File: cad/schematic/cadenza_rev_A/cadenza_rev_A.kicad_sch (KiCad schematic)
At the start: 0 parts

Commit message: added the PCB outline first proposal for the part selection
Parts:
- added J1: USB_B, Connector_USB:USB_B_Amphenol_MUSB-D511_Vertical_Rugged, symbol Connector:USB_B
- added U1, U11, U3, U5, U7, U9: TLC5916, Package_SO:TSSOP-16_4.4x5mm_P0.65mm, symbol Driver_LED:TLC5916
- added U10, U12, U2, U4, U6, U8: HDSP-A151, Display_7Segment:HDSP-A151, symbol Display_Character:HDSP-A151
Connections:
- new net: U4.1 (CA), U4.6 (CA)
- new net: U3.5 (~{OUT0}), U4.10 (A)
- new net: U3.10 (~{OUT5}), U4.2 (F)
- new net: U3.11 (~{OUT6}), U4.3 (G)
- new net: U3.9 (~{OUT4}), U4.4 (E)
- new net: U3.8 (~{OUT3}), U4.5 (D)
- new net: U3.12 (~{OUT7}), U4.7 (DP)
- new net: U3.7 (~{OUT2}), U4.8 (C)
- new net: U3.6 (~{OUT1}), U4.9 (B)
- new net: U10.2 (F), U9.10 (~{OUT5})
- new net: U10.3 (G), U9.11 (~{OUT6})
- new net: U10.7 (DP), U9.12 (~{OUT7})
- new net: U1.16 (VDD), U11.16 (VDD), U3.16 (VDD), U5.16 (VDD), U7.16 (VDD), U9.16 (VDD)
- new net: U10.10 (A), U9.5 (~{OUT0})
- new net: U10.9 (B), U9.6 (~{OUT1})
- new net: U10.8 (C), U9.7 (~{OUT2})
- new net: U10.5 (D), U9.8 (~{OUT3})
- new net: U10.4 (E), U9.9 (~{OUT4})
- new net: U7.10 (~{OUT5}), U8.2 (F)
- new net: U7.11 (~{OUT6}), U8.3 (G)
- new net: U7.12 (~{OUT7}), U8.7 (DP)
- new net: U7.5 (~{OUT0}), U8.10 (A)
- new net: U7.6 (~{OUT1}), U8.9 (B)
- new net: U7.7 (~{OUT2}), U8.8 (C)
- new net: U7.8 (~{OUT3}), U8.5 (D)
- new net: U7.9 (~{OUT4}), U8.4 (E)
- new net: U8.1 (CA), U8.6 (CA)
- new net: U6.1 (CA), U6.6 (CA)
- new net: U5.5 (~{OUT0}), U6.10 (A)
- new net: U5.10 (~{OUT5}), U6.2 (F)
- new net: U5.11 (~{OUT6}), U6.3 (G)
- new net: U5.9 (~{OUT4}), U6.4 (E)
- new net: U5.8 (~{OUT3}), U6.5 (D)
- new net: U5.12 (~{OUT7}), U6.7 (DP)
- new net: U5.7 (~{OUT2}), U6.8 (C)
- new net: U5.6 (~{OUT1}), U6.9 (B)
- new net: U1.10 (~{OUT5}), U2.2 (F)
- new net: U1.11 (~{OUT6}), U2.3 (G)
- new net: U1.12 (~{OUT7}), U2.7 (DP)
- new net: U1.5 (~{OUT0}), U2.10 (A)
- new net: U1.6 (~{OUT1}), U2.9 (B)
- new net: U1.7 (~{OUT2}), U2.8 (C)
- new net: U1.8 (~{OUT3}), U2.5 (D)
- new net: U1.9 (~{OUT4}), U2.4 (E)
- new net: U2.1 (CA), U2.6 (CA)
- new net: U12.1 (CA), U12.6 (CA)
- new net: U11.5 (~{OUT0}), U12.10 (A)
- new net: U11.10 (~{OUT5}), U12.2 (F)
- new net: U11.11 (~{OUT6}), U12.3 (G)
- new net: U11.9 (~{OUT4}), U12.4 (E)
- new net: U11.8 (~{OUT3}), U12.5 (D)
- new net: U11.12 (~{OUT7}), U12.7 (DP)
- new net: U11.7 (~{OUT2}), U12.8 (C)
- new net: U11.6 (~{OUT1}), U12.9 (B)
- new net: U10.1 (CA), U10.6 (CA)

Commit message: added the MCU 7seg routing solution
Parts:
- removed J1: USB_B, Connector_USB:USB_B_Amphenol_MUSB-D511_Vertical_Rugged, symbol Connector:USB_B
- removed U11: TLC5916, Package_SO:TSSOP-16_4.4x5mm_P0.65mm, symbol Driver_LED:TLC5916
- added J1: USB_A, Connector_USB:USB_A_Molex_105057_Vertical, symbol Connector:USB_A
- added J2: USB_C_Receptacle, Connector_USB:USB_C_Receptacle_Amphenol_12401548E4-2A_CircularHoles, symbol Connector:USB_C_Receptacle
- added U13: STM32F105RCTx, Package_QFP:LQFP-64_10x10mm_P0.5mm, symbol MCU_ST_STM32F1:STM32F105RCTx
- added U14: INA193, Package_TO_SOT_SMD:SOT-23-5, symbol Amplifier_Current:INA193
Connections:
- net at U4.10 (A): no longer U3.5 (~{OUT0})
- net at U4.2 (F): no longer U3.10 (~{OUT5})
- net at U4.3 (G): no longer U3.11 (~{OUT6})
- net at U4.4 (E): no longer U3.9 (~{OUT4})
- net at U4.5 (D): no longer U3.8 (~{OUT3})
- net at U4.8 (C): no longer U3.7 (~{OUT2})
- net at U4.9 (B): no longer U3.6 (~{OUT1})
- net GND: now reaches U1.1 (GND)
- net GND: now also J2.A1 (GND), J2.A12 (GND), J2.B1 (GND), J2.B12 (GND)
- net at U1.10 (~{OUT5}): now also U2.9 (B); no longer U2.2 (F)
- net at U1.11 (~{OUT6}): now also U2.8 (C); no longer U2.3 (G)
- net at U1.5 (~{OUT0}): no longer U2.10 (A)
- net at U1.6 (~{OUT1}): now also U2.4 (E); no longer U2.9 (B)
- net at U1.7 (~{OUT2}): now also U2.3 (G); no longer U2.8 (C)
- net at U1.8 (~{OUT3}): now also U2.2 (F); no longer U2.5 (D)
- net at U1.9 (~{OUT4}): now also U2.10 (A); no longer U2.4 (E)
- new net: U13.18 (VSS), U13.31 (VSS), U13.47 (VSS), U13.63 (VSS)
- new net: J2.A4 (VBUS), J2.A9 (VBUS), J2.B4 (VBUS), J2.B9 (VBUS)

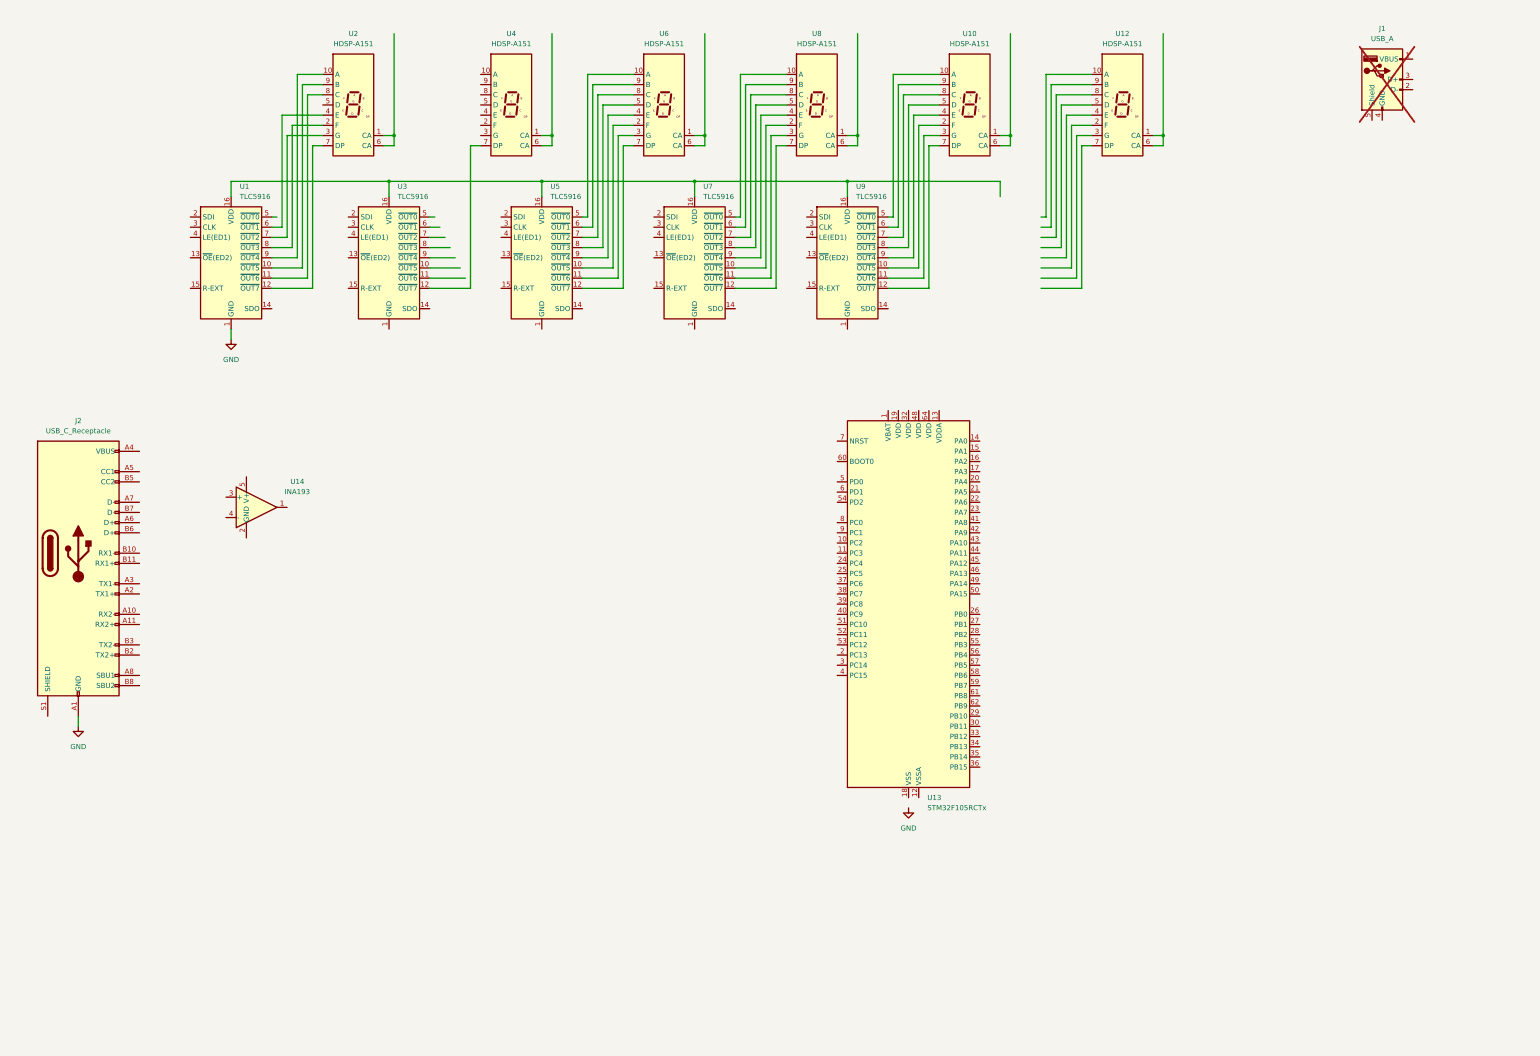
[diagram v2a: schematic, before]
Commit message: added missing parts added buzzer interface
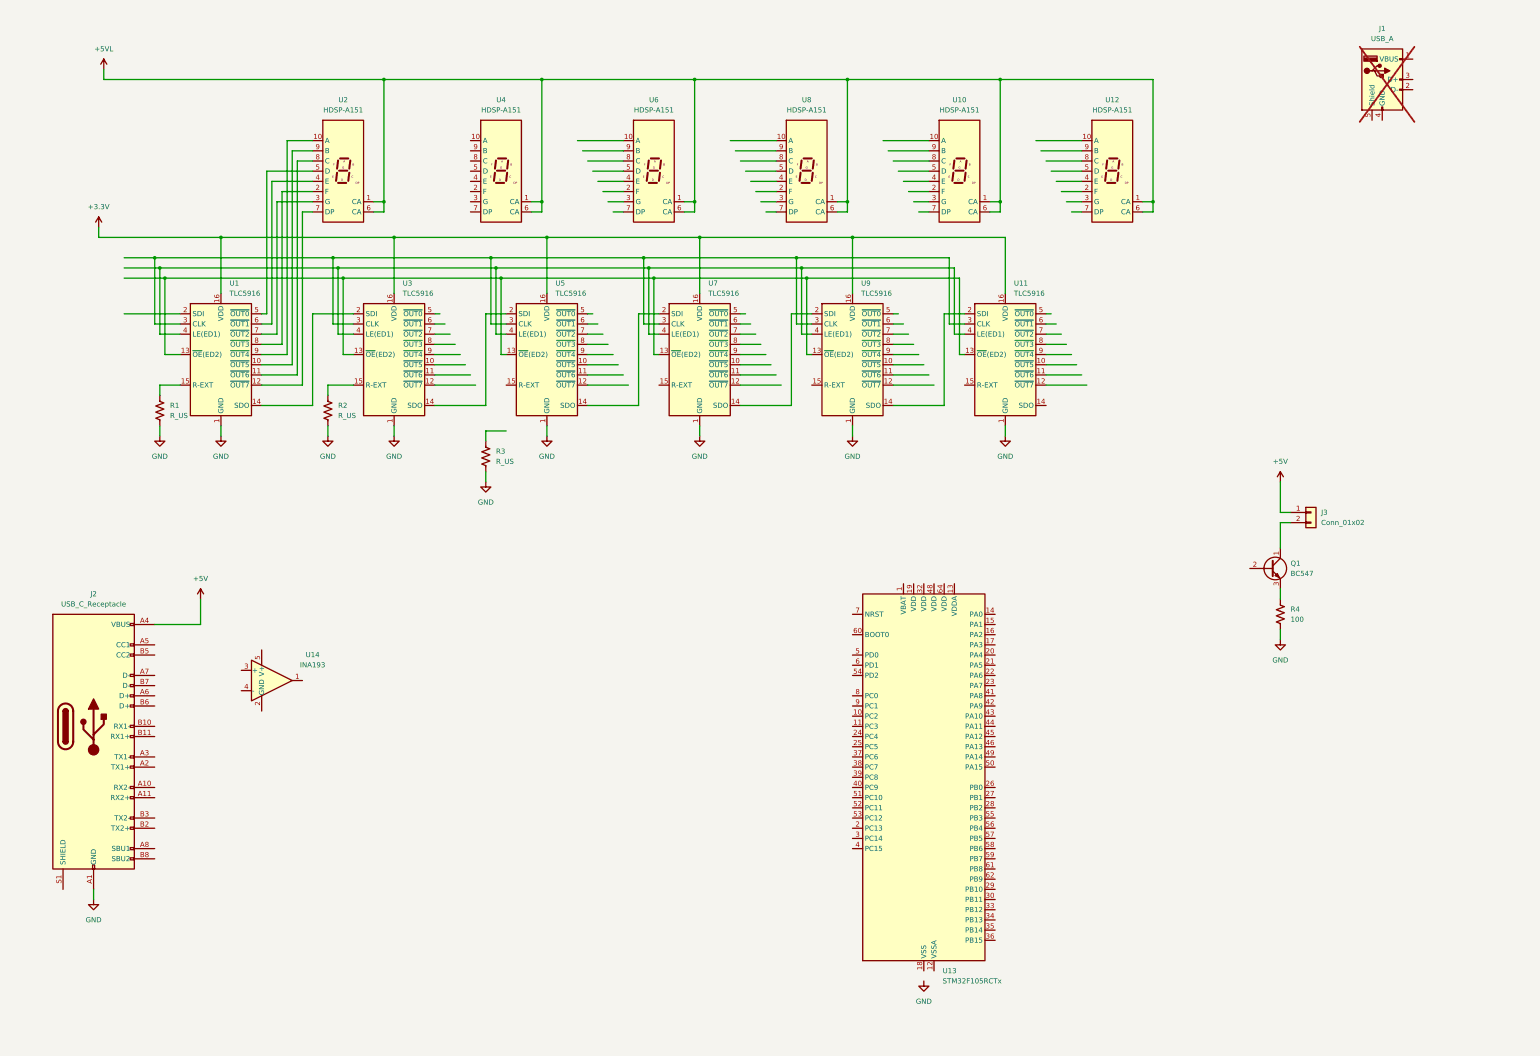
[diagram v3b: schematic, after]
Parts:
- added J3: Conn_01x02, Connector_PinHeader_2.54mm:PinHeader_1x02_P2.54mm_Vertical, symbol Connector_Generic:Conn_01x02
- added Q1: BC547, Package_TO_SOT_THT:TO-92L_HandSolder, symbol Transistor_BJT:BC547
- added R1, R2, R3: R_US, Resistor_SMD:R_0805_2012Metric_Pad1.20x1.40mm_HandSolder, symbol Device:R_US
- added R4: 100, Resistor_SMD:R_0805_2012Metric_Pad1.20x1.40mm_HandSolder, symbol Device:R_US
- added U11: TLC5916, Package_SO:TSSOP-16_4.4x5mm_P0.65mm, symbol Driver_LED:TLC5916
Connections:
- net GND: now also U3.1 (GND), U5.1 (GND), U7.1 (GND), U9.1 (GND), R1.2, R2.2, R3.2, R4.2, U11.1 (GND)
- net +5VL: now reaches U4.1 (CA), U4.6 (CA)
- net +5VL: now also U10.1 (CA), U10.6 (CA), U12.1 (CA), U12.6 (CA), U2.1 (CA), U2.6 (CA), U6.1 (CA), U6.6 (CA), U8.1 (CA), U8.6 (CA)
- net at U4.7 (DP): no longer U3.12 (~{OUT7})
- net at U9.10 (~{OUT5}): no longer U10.2 (F)
- net at U9.11 (~{OUT6}): no longer U10.3 (G)
- net at U9.12 (~{OUT7}): no longer U10.7 (DP)
- net at U9.13 (~{OE}(ED2)): now also U1.13 (~{OE}(ED2)), U3.13 (~{OE}(ED2)), U5.13 (~{OE}(ED2)), U7.13 (~{OE}(ED2)), U11.13 (~{OE}(ED2))
- net at U9.14 (SDO): now also U11.2 (SDI)
- net +3.3V: now reaches U1.16 (VDD), U3.16 (VDD), U5.16 (VDD), U7.16 (VDD), U9.16 (VDD)
- net +3.3V: now also U11.16 (VDD)
- net at U9.2 (SDI): now also U7.14 (SDO)
- net at U9.3 (CLK): now also U1.3 (CLK), U3.3 (CLK), U5.3 (CLK), U7.3 (CLK), U11.3 (CLK)
- net at U9.4 (LE(ED1)): now also U1.4 (LE(ED1)), U3.4 (LE(ED1)), U5.4 (LE(ED1)), U7.4 (LE(ED1)), U11.4 (LE(ED1))
- net at U9.5 (~{OUT0}): no longer U10.10 (A)
- net at U9.6 (~{OUT1}): no longer U10.9 (B)
- net at U9.7 (~{OUT2}): no longer U10.8 (C)
- net at U9.8 (~{OUT3}): no longer U10.5 (D)
- net at U9.9 (~{OUT4}): no longer U10.4 (E)
- net at U7.10 (~{OUT5}): no longer U8.2 (F)
- net at U7.11 (~{OUT6}): no longer U8.3 (G)
- net at U7.12 (~{OUT7}): no longer U8.7 (DP)
- net at U7.2 (SDI): now also U5.14 (SDO)
- net at U7.5 (~{OUT0}): no longer U8.10 (A)
- net at U7.6 (~{OUT1}): no longer U8.9 (B)
- net at U7.7 (~{OUT2}): no longer U8.8 (C)
- net at U7.8 (~{OUT3}): no longer U8.5 (D)
- net at U7.9 (~{OUT4}): no longer U8.4 (E)
- net at U6.10 (A): no longer U5.5 (~{OUT0})
- net at U6.2 (F): no longer U5.10 (~{OUT5})
- net at U6.3 (G): no longer U5.11 (~{OUT6})
- net at U6.4 (E): no longer U5.9 (~{OUT4})
- net at U6.5 (D): no longer U5.8 (~{OUT3})
- net at U6.7 (DP): no longer U5.12 (~{OUT7})
- net at U6.8 (C): no longer U5.7 (~{OUT2})
- net at U6.9 (B): no longer U5.6 (~{OUT1})
- net at U1.14 (SDO): now also U3.2 (SDI)
- net at U1.15 (R-EXT): now also R1.1
- net at U1.5 (~{OUT0}): now also U2.5 (D)
- net at U3.14 (SDO): now also U5.2 (SDI)
- net at U3.15 (R-EXT): now also R2.1
- net +5V: now reaches J2.A4 (VBUS), J2.A9 (VBUS), J2.B4 (VBUS), J2.B9 (VBUS)
- net +5V: now also J3.1 (Pin_1)
- new net: Q1.3 (E), R4.1
- new net: J3.2 (Pin_2), Q1.1 (C)
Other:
- moved on the sheet: J2, U1, U10, U12, U13, U14, U2, U3, U4, U5, U6, U7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

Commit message: added the LEDs to indicate the acceleration
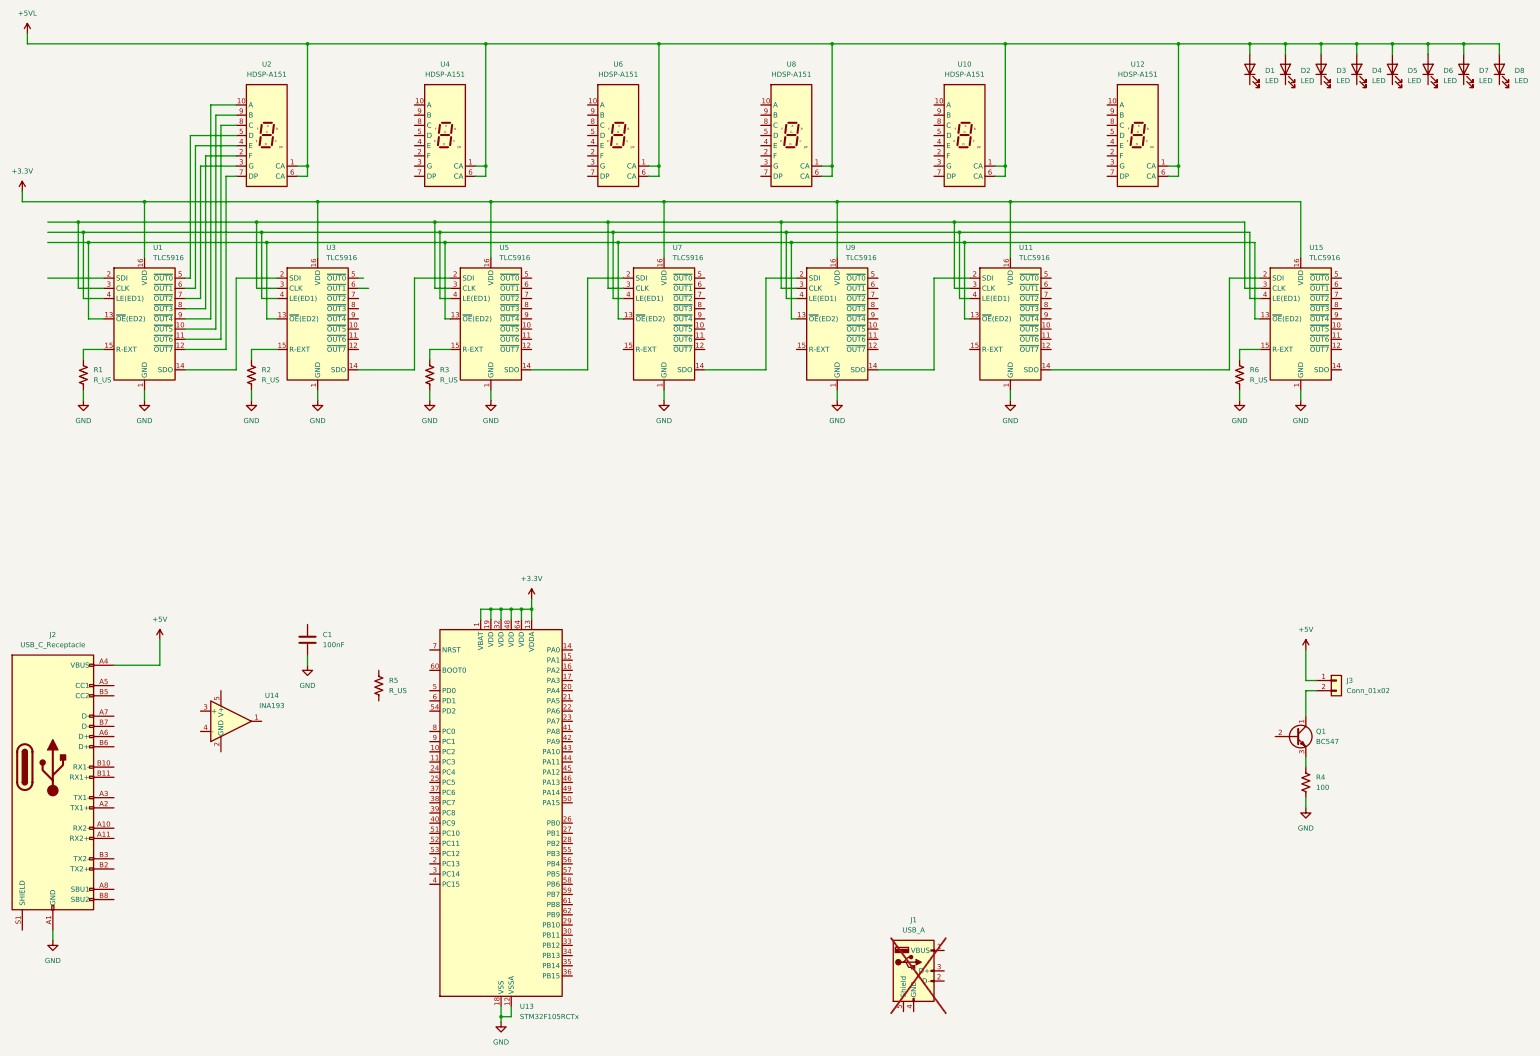
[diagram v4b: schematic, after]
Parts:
- added C1: 100nF, Capacitor_SMD:C_0805_2012Metric_Pad1.18x1.45mm_HandSolder, symbol Device:C
- added D1, D2, D3, D4, D5, D6, D7, D8: LED, LED_THT:LED_D3.0mm, symbol Device:LED
- added R5, R6: R_US, Resistor_SMD:R_0805_2012Metric_Pad1.20x1.40mm_HandSolder, symbol Device:R_US
- added U15: TLC5916, Package_SO:TSSOP-16_4.4x5mm_P0.65mm, symbol Driver_LED:TLC5916
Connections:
- net +3.3V: now also U13.1 (VBAT), U13.13 (VDDA), U13.19 (VDD), U13.32 (VDD), U13.48 (VDD), U13.64 (VDD), U15.16 (VDD)
- net +5VL: now also D1.2 (A), D2.2 (A), D3.2 (A), D4.2 (A), D5.2 (A), D6.2 (A), D7.2 (A), D8.2 (A)
- net GND: now also U13.12 (VSSA), U13.18 (VSS), U13.31 (VSS), U13.47 (VSS), U13.63 (VSS), C1.2, R6.2, U15.1 (GND)
- net at U1.13 (~{OE}(ED2)), U11.13 (~{OE}(ED2)), U3.13 (~{OE}(ED2))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: now also U15.13 (~{OE}(ED2))
- net at U1.3 (CLK), U11.3 (CLK), U3.3 (CLK)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: now also U15.3 (CLK)
- net at U1.4 (LE(ED1)), U11.4 (LE(ED1)), U3.4 (LE(ED1))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: now also U15.4 (LE(ED1))
- net at U11.14 (SDO): now also U15.2 (SDI)
- net at R3.1: now also U5.15 (R-EXT)
- new net: R6.1, U15.15 (R-EXT)
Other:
- moved on the sheet: J1, J2, J3, Q1, R1, R2, R3, R4, U1, U10, U11, U12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

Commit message: upgraded to kicad 10
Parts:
- added C2: 100nF, Capacitor_SMD:C_0805_2012Metric_Pad1.18x1.45mm_HandSolder, symbol Device:C
- added R7: 0.01, Resistor_SMD:R_1210_3225Metric_Pad1.30x2.65mm_HandSolder, symbol Device:R_US
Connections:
- net +3.3V: now also C1.1, U13.7 (NRST), U14.5 (V+), C2.1
- net +5V: now also U14.4 (-), R7.2; no longer J2.A4 (VBUS), J2.A9 (VBUS), J2.B4 (VBUS), J2.B9 (VBUS)
- net GND: now also R5.2, U14.2 (GND), C2.2
- net at U4.7 (DP): now also U3.12 (~{OUT7})
- net at U13.60 (BOOT0): now also R5.1
- net at U14.3 (+): now also J2.A4 (VBUS), J2.A9 (VBUS), J2.B4 (VBUS), J2.B9 (VBUS), R7.1
- net at D8.1 (K): now also U15.12 (~{OUT7})
- net at U15.10 (~{OUT5}): now also D6.1 (K)
- net at U15.11 (~{OUT6}): now also D7.1 (K)
- net at U15.5 (~{OUT0}): now also D1.1 (K)
- net at U15.6 (~{OUT1}): now also D2.1 (K)
- net at U15.7 (~{OUT2}): now also D3.1 (K)
- net at U15.8 (~{OUT3}): now also D4.1 (K)
- net at U15.9 (~{OUT4}): now also D5.1 (K)
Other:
- moved on the sheet: C1, R5, U13, U14
